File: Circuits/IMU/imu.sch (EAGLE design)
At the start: 11 parts, among them U1 LSM9DS1

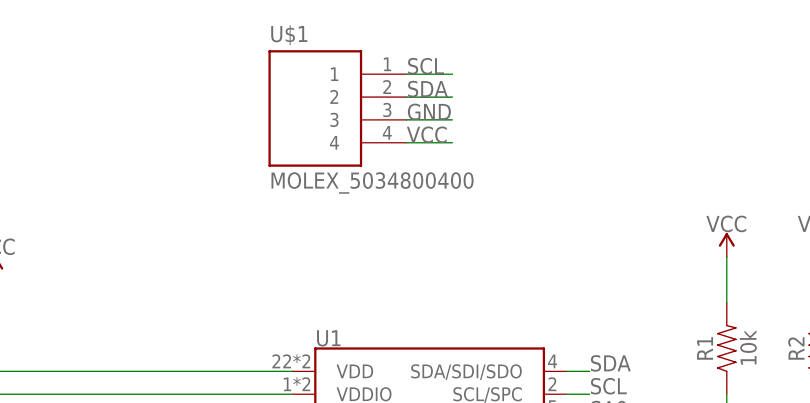
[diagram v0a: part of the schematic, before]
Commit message: Update board/schematic/custom library with 1 mm pitch connector
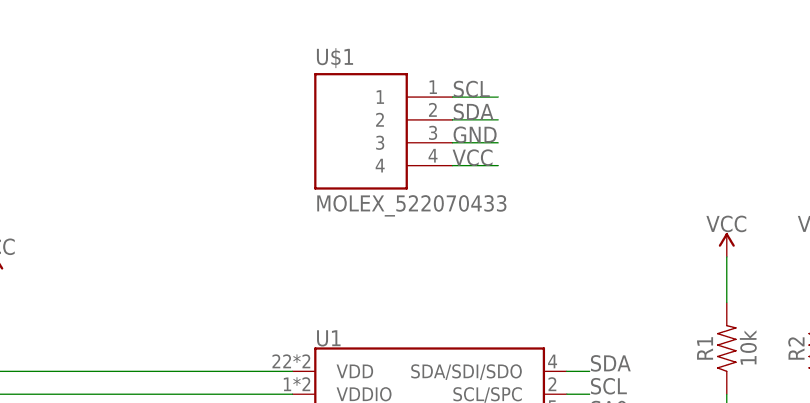
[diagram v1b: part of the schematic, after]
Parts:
- U$1: value MOLEX_5034800400 -> MOLEX_522070433; device custom:MOLEX_5034800400 -> custom:MOLEX_522070433
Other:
- moved on the sheet: U$1
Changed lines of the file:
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@@
 <part name="R3" library="SparkFun-Resistors" deviceset="10KOHM" device="-0603-1/10W-1%" value="10k"/>
 <part name="R4" library="SparkFun-Resistors" deviceset="10KOHM" device="-0603-1/10W-1%" value="10k"/>
-<part name="U$1" library="custom" deviceset="MOLEX_5034800400" device=""/>
+<part name="U$1" library="custom" deviceset="MOLEX_522070433" device=""/>
 </parts>
 <sheets>
@@
 <attribute name="VALUE" x="131.064" y="81.28" size="1.778" layer="96" font="vector" rot="R90" align="top-center"/>
 </instance>
-<instance part="U$1" gate="G$1" x="53.34" y="106.68" smashed="yes">
-<attribute name="NAME" x="48.249140625" y="115.334459375" size="1.781809375" layer="95"/>
-<attribute name="VALUE" x="48.25661875" y="99.0516" size="1.779190625" layer="96"/>
+<instance part="U$1" gate="G$1" x="58.42" y="104.14" smashed="yes">
+<attribute name="NAME" x="53.329140625" y="112.794459375" size="1.781809375" layer="95"/>
+<attribute name="VALUE" x="53.33661875" y="96.5116" size="1.779190625" layer="96"/>
 </instance>
 </instances>
@@
 <segment>
 <pinref part="U$1" gate="G$1" pin="3"/>
-<wire x1="63.5" y1="106.68" x2="68.58" y2="106.68" width="0.1524" layer="91"/>
-<label x="63.5" y="106.68" size="1.778" layer="95"/>
+<wire x1="68.58" y1="104.14" x2="73.66" y2="104.14" width="0.1524" layer="91"/>
+<label x="68.58" y="104.14" size="1.778" layer="95"/>
 </segment>
 </net>
@@
 <segment>
 <pinref part="U$1" gate="G$1" pin="4"/>
-<wire x1="63.5" y1="104.14" x2="68.58" y2="104.14" width="0.1524" layer="91"/>
-<label x="63.5" y="104.14" size="1.778" layer="95"/>
+<wire x1="68.58" y1="101.6" x2="73.66" y2="101.6" width="0.1524" layer="91"/>
+<label x="68.58" y="101.6" size="1.778" layer="95"/>
 </segment>
 </net>
@@
 <segment>
 <pinref part="U$1" gate="G$1" pin="2"/>
-<wire x1="63.5" y1="109.22" x2="68.58" y2="109.22" width="0.1524" layer="91"/>
-<label x="63.5" y="109.22" size="1.778" layer="95"/>
+<wire x1="68.58" y1="106.68" x2="73.66" y2="106.68" width="0.1524" layer="91"/>
+<label x="68.58" y="106.68" size="1.778" layer="95"/>
 </segment>
 </net>
@@
 <segment>
 <pinref part="U$1" gate="G$1" pin="1"/>
-<wire x1="63.5" y1="111.76" x2="68.58" y2="111.76" width="0.1524" layer="91"/>
-<label x="63.5" y="111.76" size="1.778" layer="95"/>
-</segment>
-</net>
+<wire x1="68.58" y1="109.22" x2="73.66" y2="109.22" width="0.1524" layer="91"/>
+<label x="68.58" y="109.22" size="1.778" layer="95"/>
+</segment>
+</net>
